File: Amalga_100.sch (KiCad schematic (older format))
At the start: 38 parts, among them P1 USB_B, P2 Interface, P3 IN+, P4 IN-, P5 MOTOR3, P6 MOTOR2, P7 MOTOR1, P9 CONN_6-HSWR-V2-rescue

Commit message: Mäusepiano (for Piano-Beginner) Areas tidied up new Phase- and Batterie-Connector and Benchmark for Pressfit Hall-filter back on PCB solder-jumper for choice: Resolver or Hallfilter
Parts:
- added P10: IN-, eigene_mod:redcube_250A_2, symbol Amalga_100-rescue:CONN_1-HSWR-V2-rescue
- added R18: 10k, Resistors_SMD:R_0805, symbol Amalga_100-rescue:R-RESCUE-BLDC_4-HSWR-V2-rescue
- added SYM1: SYM_ESD_Small, Symbols:ESD-Logo_13.2x12mm_SilkScreen, symbol Graphic:SYM_ESD_Small
- added SYM2: SYM_Arrow45_Tiny, Symbols:Symbol_Attention_CopperTop_Small, symbol graphic_symbols:SYM_Arrow45_Tiny
- NT1: symbol Device:Net-Tie_2 -> Amalga_100-rescue:Net-Tie_2-Device
- P3, P4, P5, P6, P7: footprint eigene_mod:redcube_250A_2 -> Mounting_Holes:MountingHole_5mm_Pad_Via
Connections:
- wire segments 129 -> 131
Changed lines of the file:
@@
 F 0 "P4" H 10180 4700 40  0000 L CNN
 F 1 "IN-" H 10100 4755 30  0001 C CNN
-F 2 "eigene_mod:redcube_250A_2" H 10100 4700 60  0001 C CNN
+F 2 "Mounting_Holes:MountingHole_5mm_Pad_Via" H 10100 4700 60  0001 C CNN
 F 3 "" H 10100 4700 60  0001 C CNN
 	1    10100 4700
@@
 F 0 "P3" H 10180 4500 40  0000 L CNN
 F 1 "IN+" H 10100 4555 30  0001 C CNN
-F 2 "eigene_mod:redcube_250A_2" H 10100 4500 60  0001 C CNN
+F 2 "Mounting_Holes:MountingHole_5mm_Pad_Via" H 10100 4500 60  0001 C CNN
 F 3 "" H 10100 4500 60  0001 C CNN
 	1    10100 4500
@@
 F 0 "P5" H 10150 2500 40  0000 L CNN
 F 1 "MOTOR3" H 10200 2505 30  0001 C CNN
-F 2 "eigene_mod:redcube_250A_2" H 10200 2450 60  0001 C CNN
+F 2 "Mounting_Holes:MountingHole_5mm_Pad_Via" H 10200 2450 60  0001 C CNN
 F 3 "" H 10200 2450 60  0001 C CNN
 	1    10200 2450
@@
 F 0 "P6" H 10150 2650 40  0000 L CNN
 F 1 "MOTOR2" H 10200 2655 30  0001 C CNN
-F 2 "eigene_mod:redcube_250A_2" H 10200 2600 60  0001 C CNN
+F 2 "Mounting_Holes:MountingHole_5mm_Pad_Via" H 10200 2600 60  0001 C CNN
 F 3 "" H 10200 2600 60  0001 C CNN
 	1    10200 2600
@@
 F 0 "P7" H 10150 2800 40  0000 L CNN
 F 1 "MOTOR1" H 10200 2805 30  0001 C CNN
-F 2 "eigene_mod:redcube_250A_2" H 10200 2750 60  0001 C CNN
+F 2 "Mounting_Holes:MountingHole_5mm_Pad_Via" H 10200 2750 60  0001 C CNN
 F 3 "" H 10200 2750 60  0001 C CNN
 	1    10200 2750
@@
 dir(enc)
 $Comp
-L Device:Net-Tie_2 NT1
+L Amalga_100-rescue:Net-Tie_2-Device NT1
 U 1 1 5CB51E34
 P 8800 4700
@@
 	8550 5450 8550 5700
 $Comp
-L Graphic:SYM_ESD_Small #SYM?
+L Graphic:SYM_ESD_Small SYM1
 U 1 1 5CCA21D9
 P 3850 2600
-F 0 "#SYM?" H 3850 2740 50  0001 C CNN
+F 0 "SYM1" H 3850 2740 50  0001 C CNN
 F 1 "SYM_ESD_Small" H 3850 2475 50  0001 C CNN
-F 2 "" H 3850 2610 50  0001 C CNN
+F 2 "Symbols:ESD-Logo_13.2x12mm_SilkScreen" H 3850 2610 50  0001 C CNN
 F 3 "~" H 3850 2610 50  0001 C CNN
 	1    3850 2600
 	1    0    0    -1
 $EndComp
+$Comp
+L Amalga_100-rescue:CONN_1-HSWR-V2-rescue P10
+U 1 1 5CB6BC4A
+P 10100 4600
+F 0 "P10" H 10180 4600 40  0000 L CNN
+F 1 "IN-" H 10100 4655 30  0001 C CNN
+F 2 "eigene_mod:redcube_250A_2" H 10100 4600 60  0001 C CNN
+F 3 "" H 10100 4600 60  0001 C CNN
+	1    10100 4600
+	-1   0    0    1
+$EndComp
+Wire Wire Line
+	10250 4600 10250 4700
+Connection ~ 10250 4700
+$Comp
+L graphic_symbols:SYM_Arrow45_Tiny SYM2
+U 1 1 5CB74FA7
+P 3650 2550
+F 0 "SYM2" H 3810 2600 50  0001 C CNN
+F 1 "SYM_Arrow45_Tiny" H 3650 2480 50  0001 C CNN
+F 2 "Symbols:Symbol_Attention_CopperTop_Small" H 3650 2550 50  0001 C CNN
+F 3 "~" H 3650 2550 50  0001 C CNN
+	1    3650 2550
+	1    0    0    -1
+$EndComp
+$Comp
+L Amalga_100-rescue:R-RESCUE-BLDC_4-HSWR-V2-rescue R18
+U 1 1 5CB95475
+P 3450 6750
+F 0 "R18" V 3350 6750 50  0000 C CNN
+F 1 "10k" V 3450 6750 50  0000 C CNN
+F 2 "Resistors_SMD:R_0805" H 3450 6750 60  0001 C CNN
+F 3 "" H 3450 6750 60  0001 C CNN
+	1    3450 6750
+	0    1    1    0
+$EndComp
+Wire Wire Line
+	3700 6750 3700 6650
+$Comp
+L Amalga_100-rescue:+5V-power #PWR?
+U 1 1 5CBA2946
+P 3700 6650
+AR Path="/5899E25F/5CBA2946" Ref="#PWR?"  Part="1"
+AR Path="/5C9D0FFC/5CBA2946" Ref="#PWR?"  Part="1"
+AR Path="/5CBA2946" Ref="#PWR0148"  Part="1"
+F 0 "#PWR0148" H 3700 6500 50  0001 C CNN
+F 1 "+5V" H 3700 6790 50  0000 C CNN
+F 2 "" H 3700 6650 50  0000 C CNN
+F 3 "" H 3700 6650 50  0000 C CNN
+	1    3700 6650
+	1    0    0    -1
+$EndComp
+Connection ~ 3200 6750
 $EndSCHEMATC

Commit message: made Bom (BomAmalga_Kosten.xlsx) Backup
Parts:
- SYM2: symbol graphic_symbols:SYM_Arrow45_Tiny -> Amalga_100-rescue:SYM_Arrow45_Tiny-graphic_symbols
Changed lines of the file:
@@
 Connection ~ 10250 4700
 $Comp
-L graphic_symbols:SYM_Arrow45_Tiny SYM2
+L Amalga_100-rescue:SYM_Arrow45_Tiny-graphic_symbols SYM2
 U 1 1 5CB74FA7
 P 3650 2550

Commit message: forget to check schematic
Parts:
- added MH11, MH12: MountingHole, MountingHole:MountingHole_3.2mm_M3_ISO14580_Pad, symbol Amalga_100-rescue:MountingHole-Mechanical
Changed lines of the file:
@@
 $EndComp
 Connection ~ 3200 6750
+$Comp
+L Amalga_100-rescue:MountingHole-Mechanical MH12
+U 1 1 5CB97376
+P 7250 5000
+F 0 "MH12" H 7350 5046 50  0000 L CNN
+F 1 "MountingHole" H 7350 4955 50  0000 L CNN
+F 2 "MountingHole:MountingHole_3.2mm_M3_ISO14580_Pad" H 7250 5000 50  0001 C CNN
+F 3 "~" H 7250 5000 50  0001 C CNN
+	1    7250 5000
+	1    0    0    -1
+$EndComp
+$Comp
+L Amalga_100-rescue:MountingHole-Mechanical MH11
+U 1 1 5CB9737D
+P 7250 4800
+F 0 "MH11" H 7350 4846 50  0000 L CNN
+F 1 "MountingHole" H 7350 4755 50  0000 L CNN
+F 2 "MountingHole:MountingHole_3.2mm_M3_ISO14580_Pad" H 7250 4800 50  0001 C CNN
+F 3 "~" H 7250 4800 50  0001 C CNN
+	1    7250 4800
+	1    0    0    -1
+$EndComp
 $EndSCHEMATC

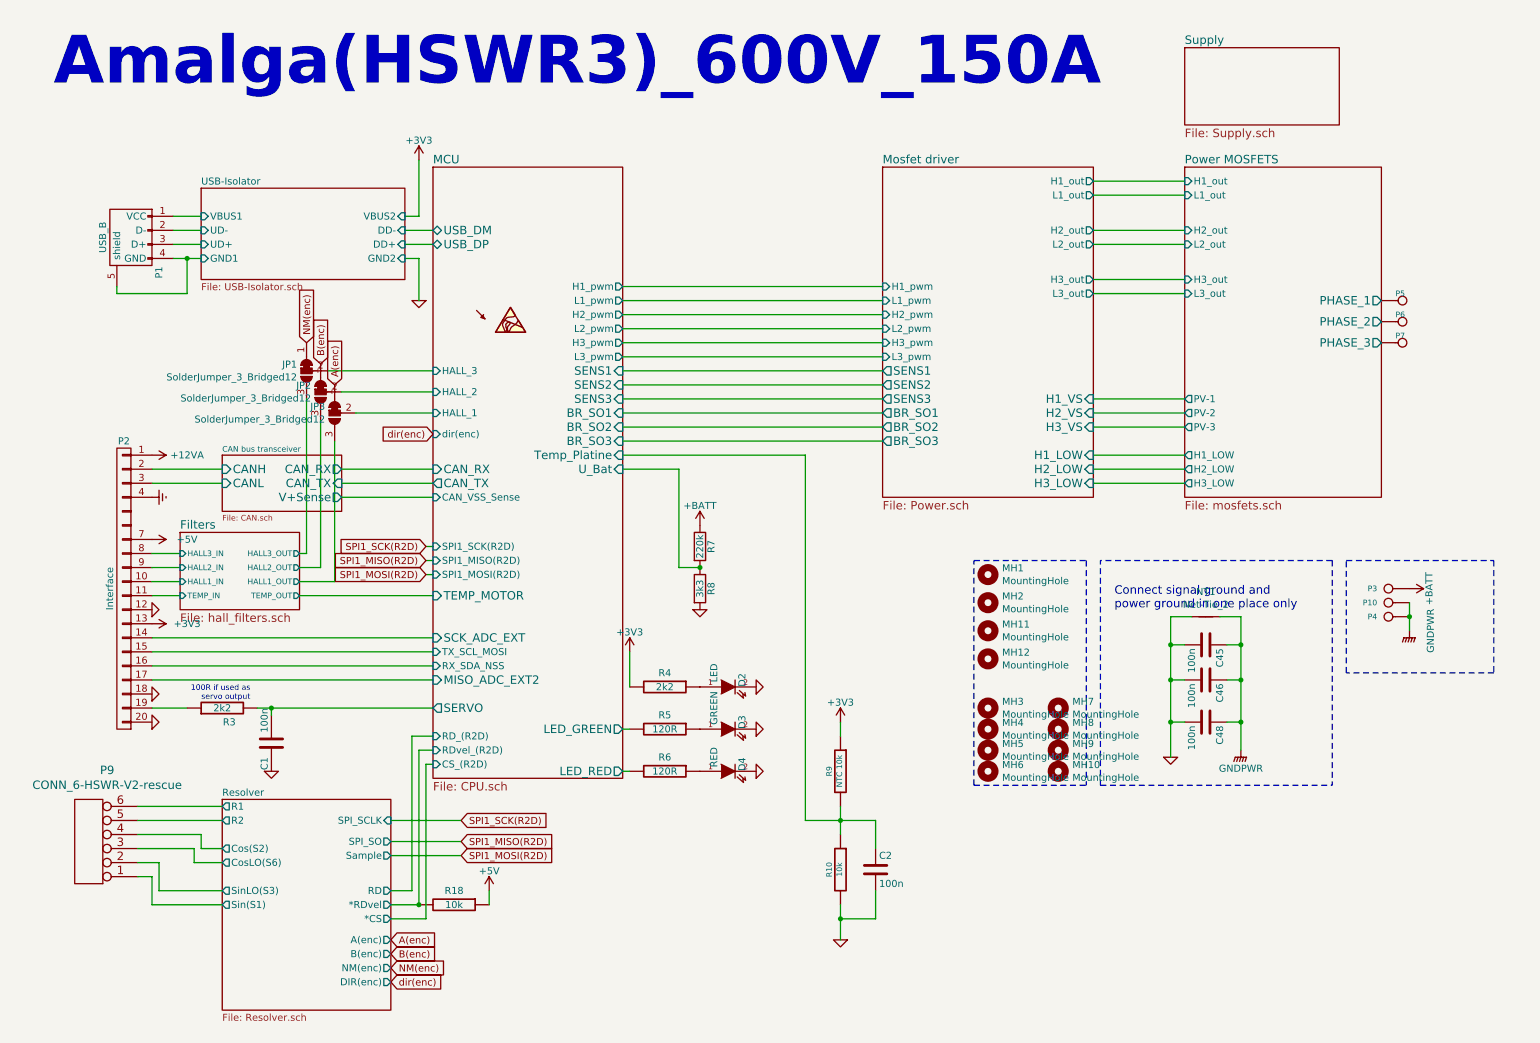
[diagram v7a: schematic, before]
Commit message: -tidied up resolver circuit (need voltage detection on reset pin. >10µs, low active)
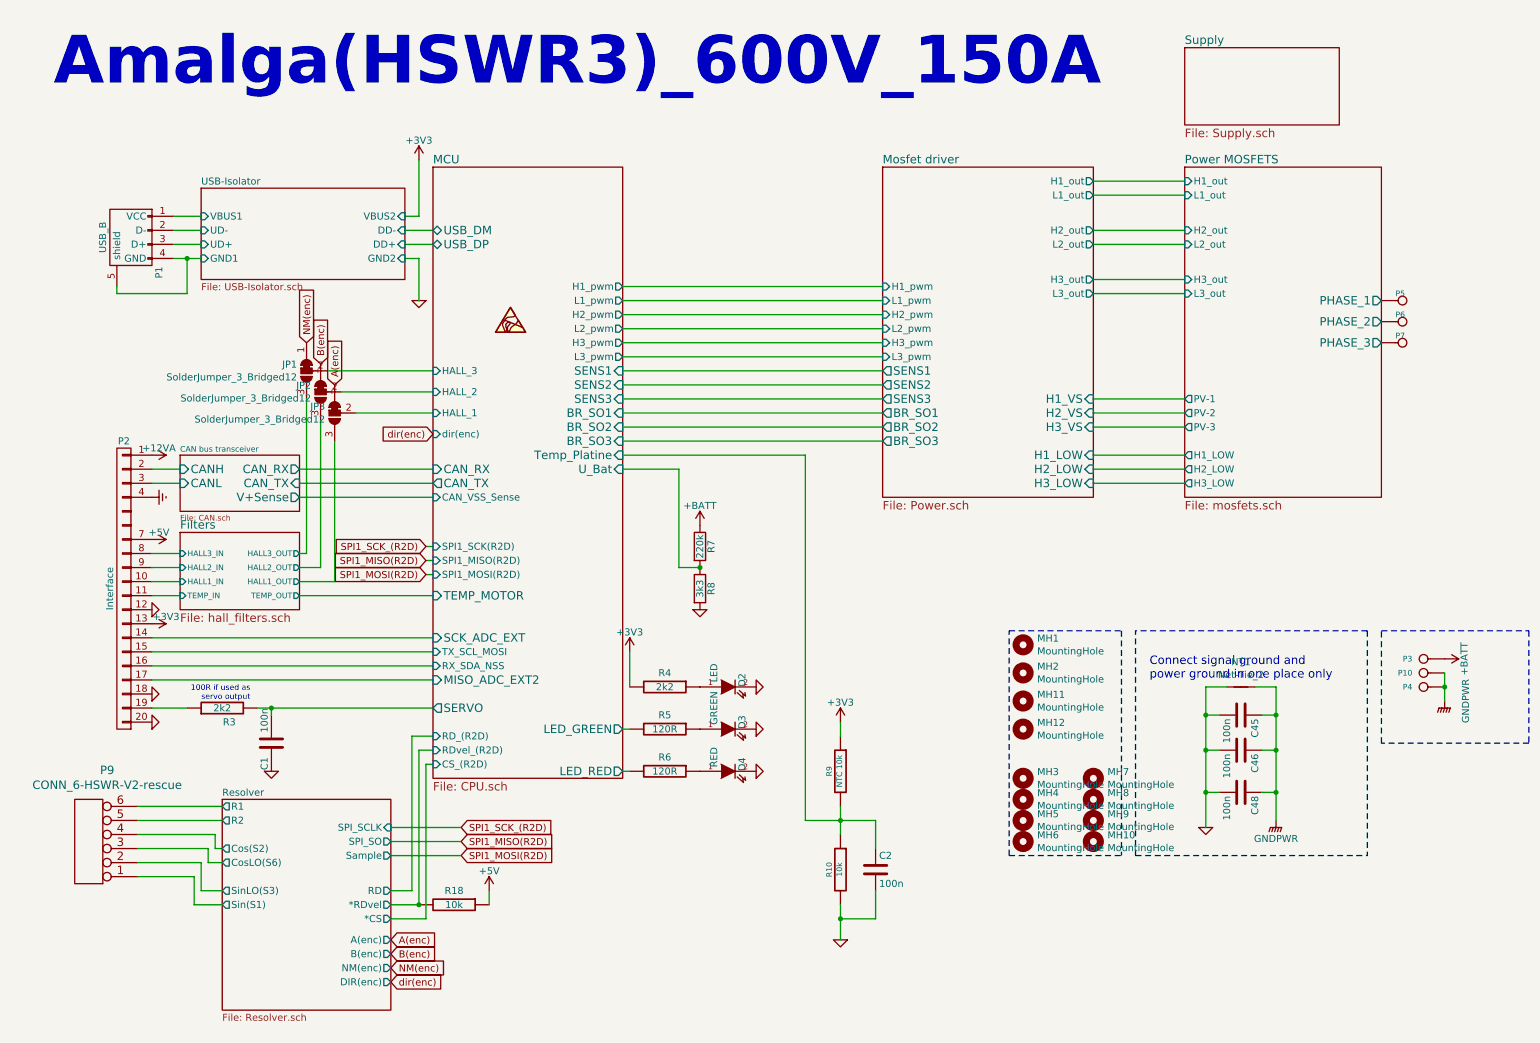
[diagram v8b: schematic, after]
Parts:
- removed SYM2: SYM_Arrow45_Tiny, Symbols:Symbol_Attention_CopperTop_Small, symbol Amalga_100-rescue:SYM_Arrow45_Tiny-graphic_symbols
- MH1, MH11, MH12, MH2: footprint MountingHole:MountingHole_3.2mm_M3_ISO14580_Pad -> Mounting_Holes:MountingHole_3.2mm_M3_ISO14580_Pad
- MH10, MH3, MH4, MH5, MH6, MH7, MH8, MH9: footprint MountingHole:MountingHole_3.2mm_M3_ISO14580 -> Mounting_Holes:MountingHole_3.2mm_M3_ISO14580
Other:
- moved on the sheet: C45, C46, C48, MH1, MH10, MH11, MH12, MH2, MH3, MH4, MH5, MH6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
